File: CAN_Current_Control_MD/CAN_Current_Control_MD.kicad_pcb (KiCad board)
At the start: 2 copper layers, 0 parts

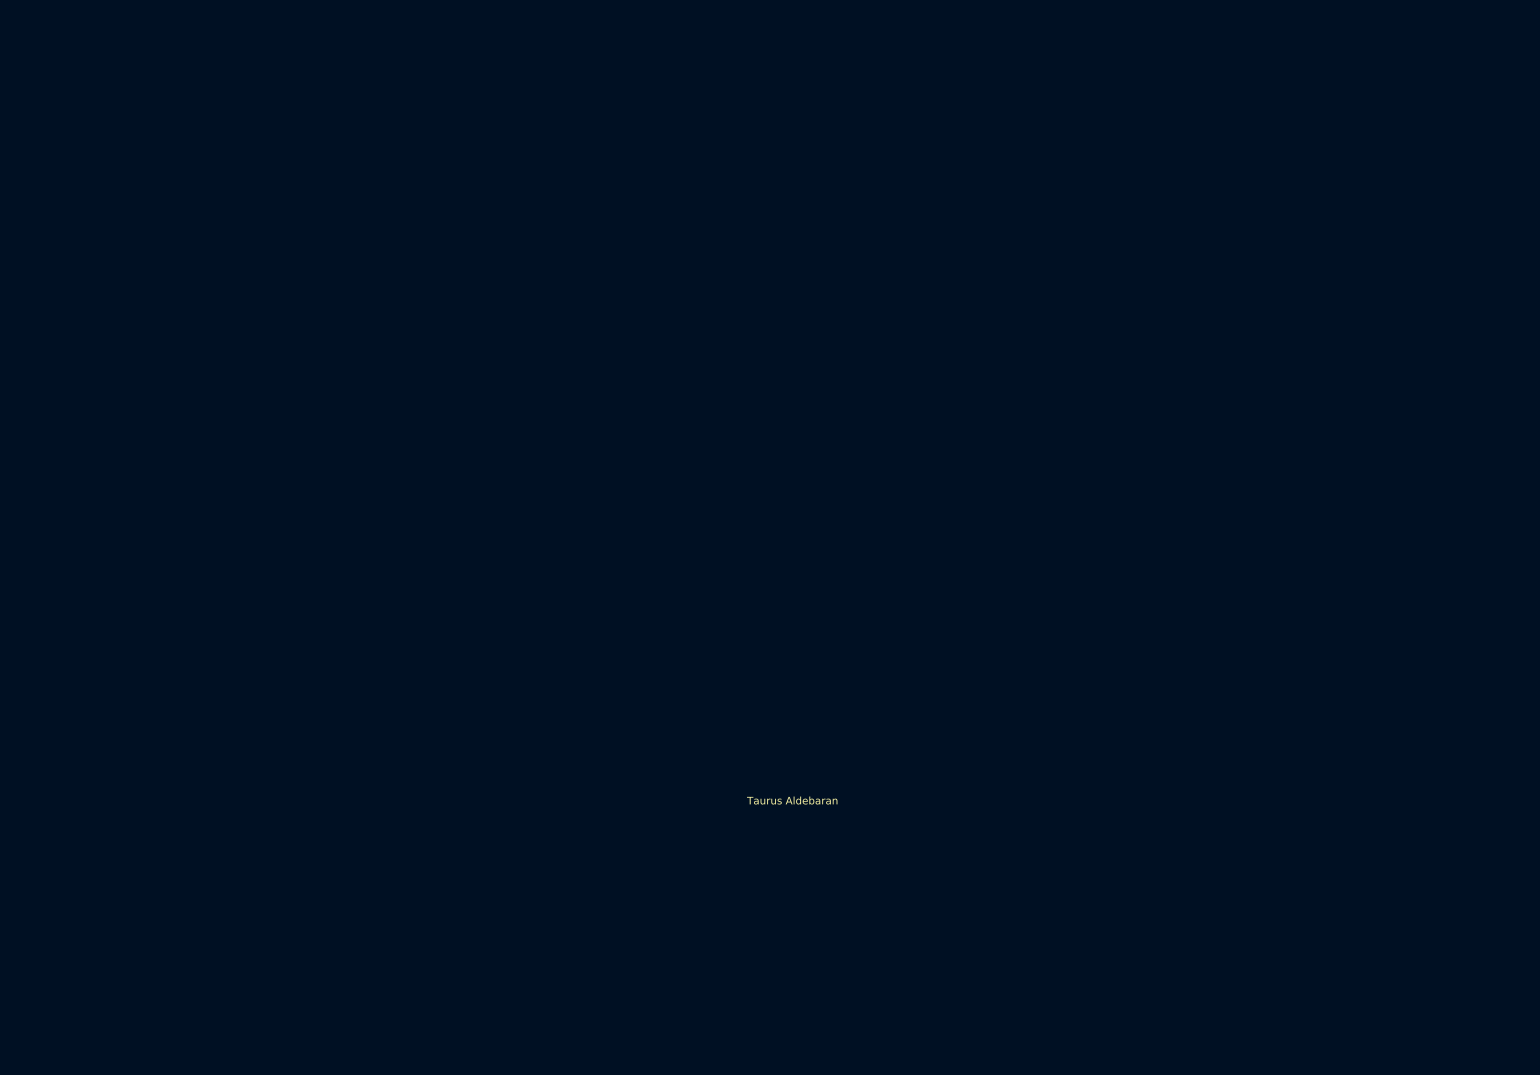
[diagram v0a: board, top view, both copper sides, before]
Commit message: 電流制御MDをだいぶ進めた
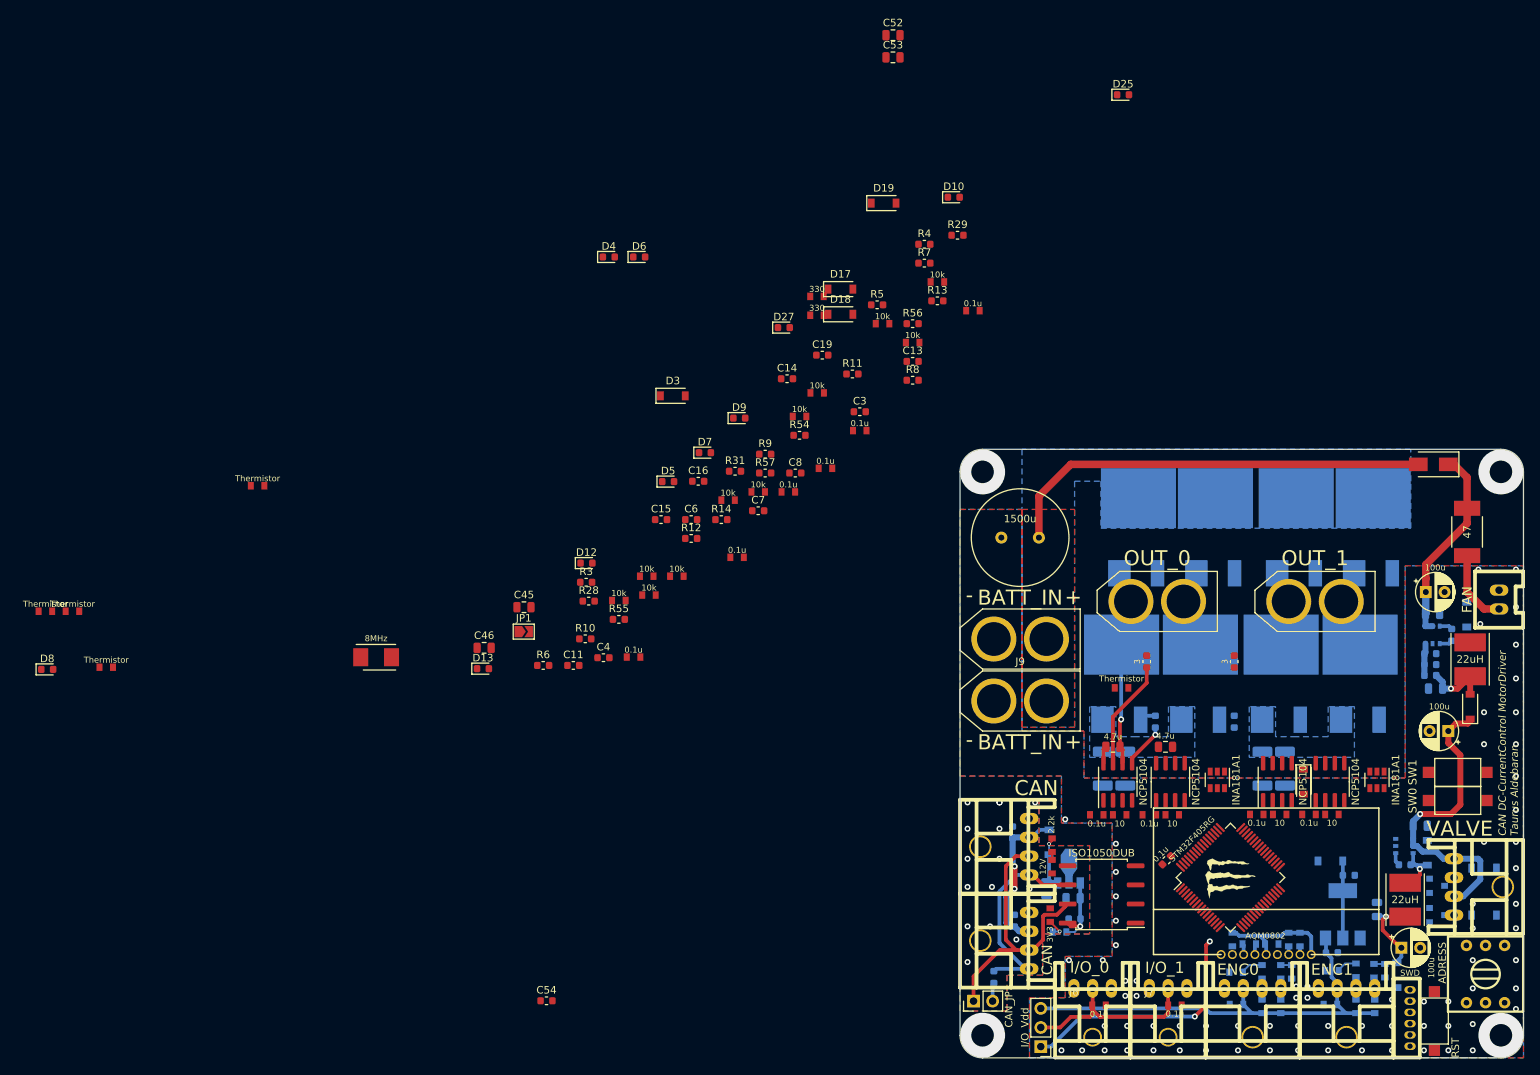
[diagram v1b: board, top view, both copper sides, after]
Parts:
- added C1: 0.1u, Capacitor_SMD:C_0603_1608Metric, B.Cu at (161.2, 126.5)
- added C10: 0.1u, Capacitor_SMD:C_0603_1608Metric, B.Cu at (153.0, 115.0)
- added C11: 0.1u, Capacitor_SMD:C_0603_1608Metric, F.Cu at (94.5, 92.8)
- added C12: 0.1u, Capacitor_SMD:C_0603_1608Metric, F.Cu at (173.5, 118.7)
- added C13: 1u, Capacitor_SMD:C_0603_1608Metric, F.Cu at (139.7, 52.3)
- added C14: 2.2u, Capacitor_SMD:C_0603_1608Metric, F.Cu at (123.0, 54.6)
- added C15: 4.7u, Capacitor_SMD:C_0603_1608Metric, F.Cu at (106.2, 73.4)
- added C16: 2.2u, Capacitor_SMD:C_0603_1608Metric, F.Cu at (111.2, 68.3)
- added C17: 10u, Capacitor_SMD:C_0603_1608Metric, B.Cu at (195.5, 131.0)
- added C18: 22u, Capacitor_SMD:C_0603_1608Metric, B.Cu at (197.8, 120.7)
- added C19: 0.1u, Capacitor_SMD:C_0603_1608Metric, F.Cu at (127.7, 51.5)
- added C2: 4.7u, Capacitor_SMD:C_0805_2012Metric, B.Cu at (157.5, 122.5)
- added C20: 0.1u, Mizz_lib:1608_WP, B.Cu at (195.3, 137.9)
- added C21: 0.1u, Mizz_lib:1608_WP, B.Cu at (182.8, 137.9)
- added C22: 0.1u, Capacitor_SMD:C_0603_1608Metric, B.Cu at (205.2, 119.3)
- added C23: 0.1u, Mizz_lib:1608_WP, F.Cu at (164.5, 138.0)
- added C24: 0.1u, Mizz_lib:1608_WP, F.Cu at (174.6, 138.0)
- added C25: 4.7u, Capacitor_SMD:C_0805_2012Metric, B.Cu at (207.2, 114.1)
- added C26: 1u, Mizz_lib:1608_WP, B.Cu at (182.2, 129.2)
- added C27: 1u, Mizz_lib:1608_WP, B.Cu at (184.5, 129.8)
- added C28: 0.1u, Mizz_lib:1608_WP, B.Cu at (187.5, 129.8)
- added C29: 10u, Capacitor_SMD:C_0805_2012Metric, B.Cu at (201.5, 125.2)
- added C3: 22p, Capacitor_SMD:C_0603_1608Metric, F.Cu at (132.7, 59.0)
- added C30: 100u, Capacitor_THT:CP_Radial_D5.0mm_P2.50mm, F.Cu at (204.8, 130.3)
- added C31: 0.1u, Mizz_lib:1608_WP, F.Cu at (132.7, 61.5)
- added C32: 0.1u, Mizz_lib:1608_WP, F.Cu at (102.5, 91.7)
- added C33: 0.1u, Mizz_lib:1608_WP, F.Cu at (147.7, 45.5)
- added C34: 0.1u, Mizz_lib:1608_WP, F.Cu at (116.3, 78.4)
- added C35: 0.1u, Mizz_lib:1608_WP, F.Cu at (128.1, 66.5)
- added C36: 0.1u, Mizz_lib:1608_WP, F.Cu at (123.1, 69.7)
- added C37: 0.1u, Capacitor_SMD:C_0603_1608Metric, B.Cu at (208.6, 92.7)
- added C38: 0.1u, Mizz_lib:1608_WP, F.Cu at (164.2, 112.7)
- added C39: 0.1u, Mizz_lib:1608_WP, F.Cu at (171.2, 112.7)
- added C4: 22p, Capacitor_SMD:C_0603_1608Metric, F.Cu at (98.5, 91.7)
- added C40: 0.1u, Mizz_lib:1608_WP, F.Cu at (185.5, 112.6)
- added C41: 0.1u, Mizz_lib:1608_WP, F.Cu at (192.4, 112.6)
- added C42: 0.1u, Capacitor_SMD:C_0603_1608Metric, B.Cu at (211.4, 88.7)
- added C43: 4.7u, Capacitor_SMD:C_0805_2012Metric, F.Cu at (166.3, 103.6)
- added C44: 4.7u, Capacitor_SMD:C_0805_2012Metric, F.Cu at (173.3, 103.6)
- added C45: 4.7u, Capacitor_SMD:C_0805_2012Metric, F.Cu at (88.0, 85.0)
- added C46: 4.7u, Capacitor_SMD:C_0805_2012Metric, F.Cu at (82.7, 90.4)
- added C47: 4.7u, Capacitor_SMD:C_0805_2012Metric, B.Cu at (208.9, 85.9)
- added C48: 100u, Capacitor_THT:CP_Radial_D5.0mm_P2.50mm, F.Cu at (208.0, 83.0)
- added C49: 10u, Capacitor_SMD:C_0805_2012Metric, B.Cu at (209.3, 95.8)
- added C5: 4.7u, Capacitor_SMD:C_0805_2012Metric, B.Cu at (161.1, 123.8)
- added C50: 100u, Capacitor_THT:CP_Radial_D5.0mm_P2.50mm, F.Cu at (211.0, 101.5)
- added C51: 1500u, Mizz_lib:C_Radial_D13mm_H25.0mm_P5.00mm, F.Cu at (156.5, 75.8)
- added C52: 4.7u, Capacitor_SMD:C_0805_2012Metric, F.Cu at (137.1, 8.88)
- added C53: 4.7u, Capacitor_SMD:C_0805_2012Metric, F.Cu at (137.1, 11.8)
- added C54: 0.1u, Capacitor_SMD:C_0603_1608Metric, F.Cu at (91.0, 137.4)
- added C6: 0.1u, Capacitor_SMD:C_0603_1608Metric, F.Cu at (110.2, 73.4)
- added C7: 0.1u, Capacitor_SMD:C_0603_1608Metric, F.Cu at (119.1, 72.2)
- added C8: 0.1u, Capacitor_SMD:C_0603_1608Metric, F.Cu at (124.1, 67.2)
- added C9: 0.1u, Capacitor_SMD:C_0603_1608Metric, B.Cu at (153.2, 126.8)
- added D1: 12V, Mizz_lib:1608_WP, F.Cu at (158.2, 119.5)
- added D10: BUS0, LED_SMD:LED_0603_1608Metric, F.Cu at (145.2, 30.4)
- added D11: DIODE, Diode_SMD:D_SOD-123, B.Cu at (157.8, 116.3)
- added D12: EMG1, LED_SMD:LED_0603_1608Metric, F.Cu at (96.3, 79.1)
- added D13: BUS1, LED_SMD:LED_0603_1608Metric, F.Cu at (82.5, 93.2)
- added D14: DIODE, Diode_SMD:D_SOD-123, B.Cu at (195.3, 118.8)
- added D15: DIODE, Diode_SMD:D_SOD-123, B.Cu at (208.2, 117.7)
- added D16: DIODE, Diode_SMD:D_SOD-123, B.Cu at (204.2, 134.0)
- added D17: DIODE, Diode_SMD:D_SOD-123, F.Cu at (130.1, 42.7)
- added D18: DIODE, Diode_SMD:D_SOD-123, F.Cu at (130.1, 46.0)
- added D19: DIODE, Diode_SMD:D_SOD-123, F.Cu at (135.8, 31.2)
- added D2: 3V3, Mizz_lib:1608_WP, F.Cu at (158.0, 126.0)
- added D20: DIODE, Diode_SMD:D_SOD-123, F.Cu at (191.7, 108.2)
- added D21: DIODE, Diode_SMD:D_SOD-123, B.Cu at (213.4, 86.0)
- added D22: DIODE, Diode_SMD:D_SOD-123, F.Cu at (213.9, 98.2)
- added D23: DIODE, Diode_SMD:D_SMA, F.Cu at (209.0, 66.0)
- added D24: DIODE, Diode_SMD:D_SOD-123, B.Cu at (215.8, 126.0)
- added D25: VALVE0, LED_SMD:LED_0603_1608Metric, F.Cu at (167.7, 16.8)
- added D26: DIODE, Diode_SMD:D_SOD-123, B.Cu at (215.8, 119.8)
- added D27: VALVE1, LED_SMD:LED_0603_1608Metric, F.Cu at (122.5, 47.8)
- added D3: DIODE, Diode_SMD:D_SOD-123, F.Cu at (107.8, 56.9)
- added D4: BATT, LED_SMD:LED_0603_1608Metric, F.Cu at (99.2, 38.4)
- added D5: MAIN_BATT, LED_SMD:LED_0603_1608Metric, F.Cu at (107.1, 68.3)
- added D6: 12VP, LED_SMD:LED_0603_1608Metric, F.Cu at (103.3, 38.4)
- added D7: 5VP, LED_SMD:LED_0603_1608Metric, F.Cu at (112.0, 64.4)
- added D8: 3V3P, LED_SMD:LED_0603_1608Metric, F.Cu at (24.5, 93.3)
- added D9: EMG0, LED_SMD:LED_0603_1608Metric, F.Cu at (116.6, 59.8)
- added J1: SWD, Mizz_lib:ZH_6P, F.Cu at (205.9, 135.9)
- added J10: FAN, Mizz_lib:XA_2P, F.Cu at (217.8, 85.2)
- added J11: OUT_0, Mizz_lib:XT60_F, F.Cu at (172.2, 84.2)
- added J12: OUT_1, Mizz_lib:XT60_F, F.Cu at (193.2, 84.2)
- added J13: VALVE, Mizz_lib:XA_4L, F.Cu at (211.8, 126.0)
- added J2: CAN, Mizz_lib:XA_4L, F.Cu at (155.2, 125.7)
- added J3: CAN, Mizz_lib:XA_4L, F.Cu at (155.2, 113.2)
- added J4: ENC0, Mizz_lib:XA_4L, F.Cu at (181.2, 135.8)
- added J5: ENC1, Mizz_lib:XA_4L, F.Cu at (193.7, 135.8)
- added J6: I/O_0, Mizz_lib:XA_3L, F.Cu at (161.2, 135.8)
- added J7: I/O_1, Mizz_lib:XA_3L, F.Cu at (171.2, 135.8)
- added J8: BATT_IN, Mizz_lib:XT60_F, F.Cu at (154.0, 97.5)
- added J9: BATT_IN, Mizz_lib:XT60_M, F.Cu at (154.0, 89.2)
- added JP1: SWD_JP, Jumper:SolderJumper-2_P1.3mm_Open_TrianglePad1.0x1.5mm, F.Cu at (87.9, 88.3)
- added JP2: CAN_JP, Connector_PinHeader_2.54mm:PinHeader_1x02_P2.54mm_Vertical, F.Cu at (147.8, 137.4)
- added JP3: I/O_Vdd, Connector_PinHeader_2.54mm:PinHeader_1x03_P2.54mm_Vertical, F.Cu at (156.8, 143.5)
- added L1: 22uH, Mizz_lib:Inductor_Taiyo-Yuden_NR-50xx_HandSoldering, F.Cu at (205.2, 124.0)
- added L2: 22uH, Mizz_lib:Inductor_Taiyo-Yuden_NR-50xx_HandSoldering, F.Cu at (213.9, 92.0)
- added Q1: MOSFET_N, Mizz_lib:D2-PAK_compact, B.Cu at (169.8, 77.5)
- added Q10: NPN, Package_TO_SOT_SMD:SOT-23, B.Cu at (209.5, 122.1)
- added Q2: MOSFET_N, Mizz_lib:D2-PAK_compact, B.Cu at (167.5, 97.0)
- added Q3: MOSFET_N, Mizz_lib:D2-PAK_compact, B.Cu at (180.0, 77.5)
- added Q4: MOSFET_N, Mizz_lib:D2-PAK_compact, B.Cu at (178.0, 97.0)
- added Q5: MOSFET_N, Mizz_lib:D2-PAK_compact, B.Cu at (190.8, 77.5)
- added Q6: MOSFET_N, Mizz_lib:D2-PAK_compact, B.Cu at (188.8, 97.0)
- added Q7: MOSFET_N, Mizz_lib:D2-PAK_compact, B.Cu at (201.0, 77.5)
- added Q8: MOSFET_N, Mizz_lib:D2-PAK_compact, B.Cu at (199.2, 97.0)
- added Q9: NPN, Package_TO_SOT_SMD:SOT-23, B.Cu at (209.5, 126.0)
- added R1: 2.2k, Mizz_lib:1608_WP, F.Cu at (158.2, 116.7)
- added R10: 10k, Resistor_SMD:R_0603_1608Metric, F.Cu at (96.1, 89.2)
- added R11: 240, Resistor_SMD:R_0603_1608Metric, F.Cu at (131.7, 54.0)
- added R12: 240, Resistor_SMD:R_0603_1608Metric, F.Cu at (110.2, 75.9)
- added R13: 240, Resistor_SMD:R_0603_1608Metric, F.Cu at (143.0, 44.2)
- added R14: 240, Resistor_SMD:R_0603_1608Metric, F.Cu at (114.2, 73.4)
- added R15: 120, Resistor_SMD:R_0603_1608Metric, B.Cu at (150.5, 134.2)
- added R16: 10k, Mizz_lib:1608_WP, B.Cu at (190.2, 133.6)
- added R17: 10k, Mizz_lib:1608_WP, B.Cu at (202.6, 133.4)
- added R18: 10k, Mizz_lib:1608_WP, B.Cu at (182.8, 133.6)
- added R19: 10k, Mizz_lib:1608_WP, B.Cu at (195.5, 133.4)
- added R2: 510, Mizz_lib:1608_WP, B.Cu at (159.2, 128.2)
- added R20: 4.7k, Mizz_lib:1608_WP, B.Cu at (188.7, 133.6)
- added R21: 4.7k, Mizz_lib:1608_WP, B.Cu at (201.1, 133.4)
- added R22: 4.7k, Mizz_lib:1608_WP, B.Cu at (186.2, 133.6)
- added R23: 4.7k, Mizz_lib:1608_WP, B.Cu at (198.7, 133.3)
- added R24: 1k, Mizz_lib:1608_WP, B.Cu at (188.7, 138.2)
- added R25: 1k, Mizz_lib:1608_WP, B.Cu at (201.2, 138.2)
- added R26: 1k, Mizz_lib:1608_WP, B.Cu at (186.2, 138.2)
- added R27: 1k, Mizz_lib:1608_WP, B.Cu at (198.7, 138.2)
- added R28: 3.9k, Resistor_SMD:R_0603_1608Metric, F.Cu at (96.6, 84.2)
- added R29: 680, Resistor_SMD:R_0603_1608Metric, F.Cu at (145.7, 35.5)
- added R3: 4.7k, Resistor_SMD:R_0603_1608Metric, F.Cu at (96.2, 81.7)
- added R30: 10k, Mizz_lib:1608_WP, B.Cu at (191.2, 129.2)
- added R31: 10k, Resistor_SMD:R_0603_1608Metric, F.Cu at (116.1, 66.9)
- added R32: 10k, Mizz_lib:1608_WP, B.Cu at (189.8, 129.2)
- added R33: 10k, Mizz_lib:1608_WP, F.Cu at (127.0, 56.5)
- added R34: 10k, Mizz_lib:1608_WP, F.Cu at (124.6, 59.6)
- added R35: 10k, Mizz_lib:1608_WP, F.Cu at (100.6, 84.1)
- added R36: 10k, Mizz_lib:1608_WP, F.Cu at (135.7, 47.3)
- added R37: 10k, Mizz_lib:1608_WP, F.Cu at (143.0, 41.7)
- added R38: 10k, Mizz_lib:1608_WP, F.Cu at (104.3, 80.9)
- added R39: 10k, Mizz_lib:1608_WP, F.Cu at (115.1, 70.8)
- added R4: 4.7k, Resistor_SMD:R_0603_1608Metric, F.Cu at (141.3, 36.7)
- added R40: 10, Mizz_lib:1608_WP, F.Cu at (167.2, 112.7)
- added R41: 10k, Mizz_lib:1608_WP, F.Cu at (139.7, 49.8)
- added R42: 10, Mizz_lib:1608_WP, F.Cu at (174.2, 112.7)
- added R43: 10k, Mizz_lib:1608_WP, F.Cu at (119.1, 69.7)
- added R44: 10, Mizz_lib:1608_WP, F.Cu at (188.6, 112.6)
- added R45: 10k, Mizz_lib:1608_WP, F.Cu at (108.3, 80.9)
- added R46: 10, Mizz_lib:1608_WP, F.Cu at (195.5, 112.6)
- added R47: 10k, Mizz_lib:1608_WP, F.Cu at (104.6, 83.4)
- added R48: 7.5k, Resistor_SMD:R_0603_1608Metric, B.Cu at (208.6, 94.1)
- added R49: 510, Resistor_SMD:R_0603_1608Metric, B.Cu at (208.6, 91.2)
- added R5: 2.2k, Resistor_SMD:R_0603_1608Metric, F.Cu at (135.0, 44.8)
- added R50: 3, Resistor_SMD:R_0603_1608Metric, F.Cu at (170.8, 92.2)
- added R51: 3, Resistor_SMD:R_0603_1608Metric, B.Cu at (172.0, 100.2)
- added R52: 3, Resistor_SMD:R_0603_1608Metric, F.Cu at (182.5, 92.2)
- added R53: 3, Resistor_SMD:R_0603_1608Metric, B.Cu at (182.5, 100.2)
- added R54: 3, Resistor_SMD:R_0603_1608Metric, F.Cu at (124.6, 62.1)
- added R55: 3, Resistor_SMD:R_0603_1608Metric, F.Cu at (100.6, 86.6)
- added R56: 3, Resistor_SMD:R_0603_1608Metric, F.Cu at (139.7, 47.3)
- added R57: 3, Resistor_SMD:R_0603_1608Metric, F.Cu at (120.1, 67.2)
- added R58: 2m, Mizz_lib:R_2010_5025Metric, B.Cu at (165.0, 106.5)
- added R59: 2m, Mizz_lib:R_2010_5025Metric, B.Cu at (186.2, 106.5)
- added R6: 510, Resistor_SMD:R_0603_1608Metric, F.Cu at (90.5, 92.8)
- added R60: 2m, Mizz_lib:R_2010_5025Metric, B.Cu at (168.0, 106.5)
- added R61: 2m, Mizz_lib:R_2010_5025Metric, B.Cu at (189.2, 106.5)
- added R62: 47, Mizz_lib:R_2812, F.Cu at (213.5, 75.0)
- added R63: 330, Mizz_lib:1608_WP, F.Cu at (127.0, 43.6)
- added R64: 330, Mizz_lib:1608_WP, F.Cu at (127.0, 46.2)
- added R7: 330, Resistor_SMD:R_0603_1608Metric, F.Cu at (141.3, 39.2)
- added R8: 10k, Resistor_SMD:R_0603_1608Metric, F.Cu at (139.7, 54.8)
- added R9: 10k, Resistor_SMD:R_0603_1608Metric, F.Cu at (120.1, 64.6)
- added SW1: SW0, Button_Switch_SMD:SW_SPST_CK_RS282G05A3, F.Cu at (212.2, 110.8)
- added SW2: SW1, Button_Switch_SMD:SW_SPST_CK_RS282G05A3, F.Cu at (212.2, 107.0)
- added SW3: RST, Button_Switch_SMD:SW_SPST_CK_RS282G05A3, F.Cu at (209.2, 140.1)
- added TH1: Thermistor, Mizz_lib:1608_WP, F.Cu at (27.9, 85.5)
- added TH2: Thermistor, Mizz_lib:1608_WP, F.Cu at (167.5, 95.8)
- added TH3: Thermistor, Mizz_lib:1608_WP, F.Cu at (52.5, 68.8)
- added TH4: Thermistor, Mizz_lib:1608_WP, F.Cu at (32.4, 93.0)
- added TH5: Thermistor, Mizz_lib:1608_WP, F.Cu at (24.2, 85.5)
- added U1: BD33FA1, Package_TO_SOT_SMD:SOT-89-3, B.Cu at (160.5, 120.2)
- added U10: NCP5104, Package_SO:SOIC-8_3.9x4.9mm_P1.27mm, F.Cu at (188.2, 108.2)
- added U11: NCP5104, Package_SO:SOIC-8_3.9x4.9mm_P1.27mm, F.Cu at (195.2, 108.2)
- added U12: BD9G101G, Package_SO:TSOP-6_1.65x3.05mm_P0.95mm, B.Cu at (208.9, 88.7)
- added U13: INA181A1, Package_TO_SOT_SMD:SOT-23-6, F.Cu at (180.2, 108.0)
- added U14: INA181A1, Package_TO_SOT_SMD:SOT-23-6, F.Cu at (201.5, 108.0)
- added U15: LOGO, Mizz_lib:Mini_Monster, F.Cu at (182.0, 121.0)
- added U2: ISO1050DUB, Package_SO:SOP-8_6.62x9.15mm_P2.54mm, F.Cu at (164.8, 123.2)
- added U3: STM32F405RG, Package_QFP:LQFP-64_10x10mm_P0.5mm, F.Cu at (182.0, 121.0)
- added U4: ADRESS, Mizz_lib:rotary_0F, F.Cu at (215.9, 133.8)
- added U5: AZ1086H, Package_TO_SOT_SMD:SOT-223-3_TabPin2, B.Cu at (196.9, 125.9)
- added U6: BD9G101G, Package_SO:TSOP-6_1.65x3.05mm_P0.95mm, B.Cu at (205.2, 116.8)
- added U7: AQM0802, Mizz_lib:AQM0802_original, F.Cu at (171.8, 111.8)
- added U8: NCP5104, Package_SO:SOIC-8_3.9x4.9mm_P1.27mm, F.Cu at (167.0, 108.2)
- added U9: NCP5104, Package_SO:SOIC-8_3.9x4.9mm_P1.27mm, F.Cu at (174.0, 108.2)
- added Y1: 8MHz, Mizz_lib:Crystal_SMD_5032_2Pads, F.Cu at (68.3, 91.7)
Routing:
- net +5VP: track 0.00 -> 59.6 mm
- net +BATT: track 0.00 -> 57.8 mm
- net +3.3VP: track 0.00 -> 49.3 mm, vias 0 -> 2
- net +12P: track 0.00 -> 41.4 mm, vias 0 -> 1
- net /CAN_H: track 0.00 -> 37.0 mm
- net /CAN_L: track 0.00 -> 27.6 mm
- net Batt: track 0.00 -> 26.3 mm
- net Net-(C23-Pad2): track 0.00 -> 25.1 mm
- net Net-(C10-Pad2): track 0.00 -> 20.6 mm, vias 0 -> 2
- net OUT0_L: track 0.00 -> 16.8 mm, vias 0 -> 1
- net Net-(R50-Pad2): track 0.00 -> 14.6 mm
- net /FB_5V: track 0.00 -> 11.5 mm, vias 0 -> 1
- net Net-(C18-Pad1): track 0.00 -> 10.3 mm
- net Net-(J10-Pad2): track 0.00 -> 10.0 mm
- net +3V3: track 0.00 -> 9.83 mm, vias 0 -> 1
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- added copper zone on B.Cu, net +BATT
- added copper zone on F.Cu, net +BATT
- added copper zone on B.Cu, net GND
- added copper zone on F.Cu, net GND
- added copper zone on B.Cu, net GNDPWR
- added copper zone on F.Cu, net GNDPWR
- added copper zone on B.Cu, net MD0_OUT
- added copper zone on B.Cu, net MD1_OUT
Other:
- board outline added: 75 x 81 mm
- board text added: "+"
- board text added: "-"
- board text added: "CAN DC-CurrentControl MotorDriver Taurus Aldebaran"
- board text removed: "Taurus Aldebaran"

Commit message: ぶざーてすときばんは頭悪い
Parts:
- C52, C53, C54, JP1, R55, R57: moved to B.Cu
- R37: value 10k -> 1k
- moved JP1 130.7 mm to (210.5, 133.5), turned to 90 degrees
- moved D6 119.6 mm to (209.5, 93.5), turned to 270 degrees
- moved C54 118.2 mm to (209.2, 139.4), turned to 270 degrees
- moved C46 112.7 mm to (194.6, 103.6)
- moved Y1 111.9 mm to (174.3, 127.5), turned to 315 degrees
- moved D5 111.2 mm to (218.0, 76.5), turned to 90 degrees
- moved C45 101.4 mm to (187.7, 103.6)
- moved R55 93.7 mm to (193.2, 100.2), turned to 270 degrees
- moved C52 92.9 mm to (154.0, 100.2), turned to 180 degrees
- moved D19 91.2 mm to (184.6, 108.2), turned to 270 degrees
- moved R57 90.0 mm to (203.8, 100.2), turned to 270 degrees
- moved R5 87.2 mm to (209.5, 90.0), turned to 270 degrees
- moved R4 85.0 mm to (218.0, 73.2), turned to 90 degrees
- moved R36 84.0 mm to (208.0, 90.0), turned to 270 degrees
- moved R37 83.1 mm to (208.0, 93.5), turned to 270 degrees
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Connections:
- D6 pad 1: GNDPWR -> Net-(D6-Pad1)
- D6 pad 2: Net-(D6-Pad2) -> +12P
- R5 pad 1: Net-(D6-Pad2) -> GNDPWR
- R5 pad 2: +12P -> Net-(D6-Pad1)
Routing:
- net Net-(R56-Pad2): track 0.00 -> 21.2 mm
- net Net-(R52-Pad2): track 0.00 -> 16.5 mm
- net GNDPWR: track 0.00 -> 16.0 mm, vias 73 -> 82
- net Net-(R53-Pad2): track 0.00 -> 9.96 mm, vias 0 -> 1
- net Net-(R57-Pad2): track 0.00 -> 9.81 mm, vias 0 -> 1
- net /~RST: track 0.00 -> 8.75 mm, vias 0 -> 1
- net +12P: track 41.4 -> 49.1 mm
- net Batt: track 26.3 -> 32.6 mm, vias 0 -> 1
- net Net-(Q7-PadG): track 0.00 -> 6.23 mm, vias 0 -> 1
- net Net-(R55-Pad2): track 0.00 -> 6.04 mm, vias 0 -> 1
- net Net-(J1-Pad2): track 0.00 -> 5.94 mm
- net Net-(C42-Pad1): track 1.75 -> 6.29 mm, vias 0 -> 1
- net OUT1_R: track 0.00 -> 2.32 mm
- net OUT0_R: track 0.00 -> 2.32 mm
- net Net-(C46-Pad1): track 0.00 -> 2.31 mm
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- added copper zone on B.Cu, net OUT0_R
- added copper zone on B.Cu, net OUT1_R
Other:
- board text added: "CAN DC-Current Motor Controller Taurus Aldebaran"
- board text removed: "CAN DC-CurrentControl MotorDriver Taurus Aldebaran"

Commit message: 配置しただけで分かるやばいやつ
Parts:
- added C55: 0.1u, Mizz_lib:1608_WP, F.Cu at (182.1, 110.7)
- added C56: 0.1u, Mizz_lib:1608_WP, F.Cu at (203.3, 110.6)
- added F1: Polyfuse, Fuse:Fuse_1812_4532Metric_Pad1.30x3.40mm_HandSolder, F.Cu at (197.3, 121.2)
- C1, C12, C17, C18, C22, C3, C4, C42, C8: footprint Capacitor_SMD:C_0603_1608Metric -> Mizz_lib:1608_WP
- C11, C13, C14, C15, C16, C19: footprint Capacitor_SMD:C_0603_1608Metric -> Mizz_lib:1608_WP; moved to B.Cu
- C32, C33, C34, C35, C36, C6, C7, R10, R29, R31, R6, R7, R8, R9: moved to B.Cu
- moved TH5 175.3 mm to (199.2, 95.8)
- moved TH1 168.8 mm to (191.8, 126.0), turned to 180 degrees
- moved D8 150.0 mm to (169.7, 131.2), turned to 180 degrees
- moved TH4 145.7 mm to (178.0, 95.8)
- moved TH3 138.9 mm to (188.8, 95.8)
- moved D13 123.1 mm to (203.2, 117.8), turned to 180 degrees
- moved D3 117.1 mm to (199.2, 130.1)
- moved R10 116.7 mm to (211.4, 107.0), turned to 180 degrees
- moved D25 116.5 mm to (208.7, 125.8), turned to 90 degrees
- moved R63 114.5 mm to (208.7, 123.8), turned to 270 degrees
- moved D12 113.2 mm to (203.2, 116.3), turned to 180 degrees
- moved D27 113.0 mm to (208.7, 120.9), turned to 90 degrees
- moved R28 111.4 mm to (201.9, 120.5), turned to 90 degrees
- moved R64 109.3 mm to (208.7, 118.8), turned to 270 degrees
- moved D10 102.4 mm to (203.2, 114.9), turned to 180 degrees
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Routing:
- net +5VP: track 59.6 -> 84.8 mm, vias 0 -> 2
- net Net-(D3-Pad2): track 0.00 -> 11.2 mm, vias 0 -> 1
- net Net-(D16-Pad1): track 0.00 -> 7.79 mm, vias 0 -> 1
- net Net-(Q7-PadG): track 6.23 -> 0.00 mm, vias 1 -> 0
- net +3.3VP: track 49.3 -> 54.5 mm
- net Net-(R56-Pad2): track 21.2 -> 16.5 mm
- net /SW1: track 0.00 -> 2.31 mm, vias 0 -> 1
- net /SW0: track 0.00 -> 2.31 mm, vias 0 -> 1
- net Net-(C42-Pad1): track 6.29 -> 8.40 mm
- net /BATTERY_VOLTAGE: track 0.15 -> 1.85 mm
- net Net-(R52-Pad2): track 16.5 -> 18.0 mm
- net GNDPWR: vias 82 -> 80
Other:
- board text added: "CAN DC-Current Motor Controller Taurus Aldebaran ver.0.0"
- board text added: "Designed by A.Mizuta in 2020/03/0."
- board text added: "V0"
- board text added: "V1"
- board text removed: "CAN DC-Current Motor Controller Taurus Aldebaran"

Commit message: もうちょいで電流制御MDの配線が終わる
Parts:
- C7: moved to F.Cu
- D10, D12, D13, D9: footprint LED_SMD:LED_0603_1608Metric -> Mizz_lib:1608_WP
- R34, R41: moved to B.Cu
- R6, R7: footprint Resistor_SMD:R_0603_1608Metric -> Mizz_lib:1608_WP
- moved R11 38.3 mm to (162.9, 114.0)
- moved R12 38.3 mm to (162.9, 115.3)
- moved R13 36.3 mm to (164.9, 116.5)
- moved R14 36.3 mm to (164.9, 117.8)
- moved D9 35.9 mm to (167.2, 113.9)
- moved D10 35.9 mm to (167.2, 115.2)
- moved D12 35.9 mm to (167.2, 116.4)
- moved D13 35.9 mm to (167.2, 117.8)
- moved C14 6.21 mm to (188.2, 122.4), turned to 315 degrees
- moved C7 3.13 mm to (184.8, 129.1), turned to 225 degrees
- moved C31 2.86 mm to (191.8, 127.3)
- moved R34 2.25 mm to (165.9, 115.3)
- moved R41 2.21 mm to (165.9, 114.1)
- moved C3 0.96 mm to (172.5, 129.2)
- moved R31 0.51 mm to (186.2, 122.5)
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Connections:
- D10 pad 1: GNDPWR -> /LED1
- D12 pad 1: GNDPWR -> /LED2
- D13 pad 1: GNDPWR -> /LED3
- D9 pad 1: GNDPWR -> /LED0
- R11 pad 1: /LED0 -> +3.3VP
- R12 pad 1: /LED1 -> +3.3VP
- R13 pad 1: /LED2 -> +3.3VP
- R14 pad 1: /LED3 -> +3.3VP
- R16 pad 2: /TIM3_CH1 -> /TIM4_CH1
- R17 pad 2: /TIM4_CH1 -> /TIM3_CH1
- R18 pad 2: /TIM3_CH2 -> /TIM4_CH2
- R19 pad 2: /TIM4_CH2 -> /TIM3_CH2
- R20 pad 2: /TIM3_CH1 -> /TIM4_CH1
- R21 pad 2: /TIM4_CH1 -> /TIM3_CH1
- R22 pad 2: /TIM3_CH2 -> /TIM4_CH2
- R23 pad 2: /TIM4_CH2 -> /TIM3_CH2
- U3 pad 10: /Current1_Analog -> /Current0_Analog
- U3 pad 11: /Current0_Analog -> /Current1_Analog
- U3 pad 38: /PWM0L -> /PWM0R
- U3 pad 39: /PWM0R -> /PWM0L
- U3 pad 40: /SW1 -> /SW0
- U3 pad 41: /SW0 -> /SW1
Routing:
- net +3.3VP: track 54.5 -> 270.2 mm, vias 2 -> 22
- net GNDPWR: track 16.0 -> 95.0 mm, vias 80 -> 94
- net /BATTERY_VOLTAGE: track 1.85 -> 58.4 mm, vias 0 -> 4
- net /MD1L_Temp: track 0.00 -> 53.1 mm, vias 0 -> 8
- net /MD0L_Temp: track 0.00 -> 50.5 mm, vias 0 -> 5
- net /MD1R_Temp: track 0.00 -> 49.1 mm, vias 0 -> 7
- net +12P: track 49.1 -> 94.8 mm, vias 1 -> 6
- net /TIM4_CH1: track 1.45 -> 44.8 mm, vias 0 -> 5
- net /~RST: track 8.75 -> 51.3 mm, vias 1 -> 3
- net /SWCLK: track 0.00 -> 41.3 mm, vias 0 -> 4
- net /SWDIO: track 0.00 -> 40.3 mm, vias 0 -> 4
- net /TIM3_CH1: track 1.45 -> 41.5 mm, vias 0 -> 1
- net /EN0: track 0.00 -> 36.8 mm, vias 0 -> 3
- net /ADRESS_2: track 0.00 -> 36.5 mm, vias 0 -> 4
- net /TIM3_CH2: track 3.00 -> 39.1 mm, vias 0 -> 1
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- added copper zone on B.Cu, net OUT0_L
- added copper zone on F.Cu, net OUT0_L
- added copper zone on F.Cu, net OUT0_R
- added copper zone on B.Cu, net OUT1_L
- added copper zone on F.Cu, net OUT1_L
- added copper zone on F.Cu, net OUT1_R
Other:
- board text added: "CAN DC-Motor Current Controller Taurus Aldebaran ver.0.0"
- board text added: "GND"
- board text added: "I/O"
- board text added: "Vdd"
- board text removed: "CAN DC-Current Motor Controller Taurus Aldebaran ver.0.0"
